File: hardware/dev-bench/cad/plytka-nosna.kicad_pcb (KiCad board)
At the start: 2 copper layers, 170 x 100 mm, 69 parts, among them J1 ARDUINO POWER, J10 CC1120EM P2, J11 ANALIZATOR, J12 VTEST 0-15V, J2 ARDUINO A0-A5, J3 ARDUINO D0-D7, J4 ARDUINO D8-SCL, J5 DEVKITC J1, J6 DEVKITC J3, J7 SHARP LS027B7DH01A, J9 CC1120EM P1, Q1 MMBT3904, SW1 GÓRA, SW2 DÓŁ, SW3 OK, SW4 WSTECZ, SW5 CISZA, SW6 PRZYGOTOWANIE, U1 CY15B104QN-50SXI, U2 MCP1640

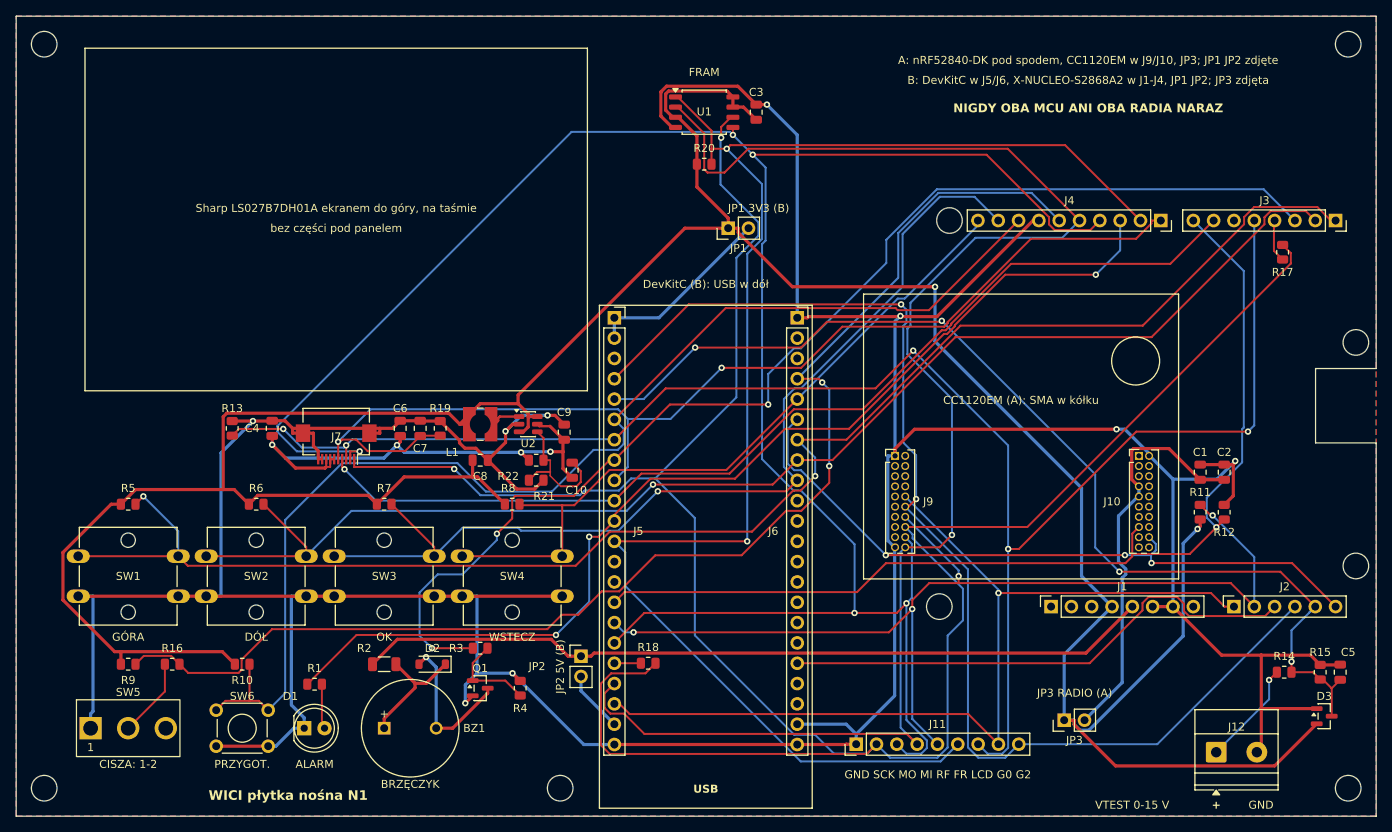
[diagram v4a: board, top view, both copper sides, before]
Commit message: Dev bench N1: hardware FRAM CS release on supply loss (audit vs F106)
The spec (elektronika.md, power loss, point 2) requires the FRAM CS to be
released before the FRAM supply drops below its minimum. The Arduino
RESET pin of the nRF52840-DK is not connected to the MCU (R45 not
fitted), so a supervisor on the MCU reset cannot do it on bench A.

- U3 TPS3840PH27 (push-pull active-high, 2.66-2.74 V) and U4 74LVC1G32
  force CS of U1 high below the threshold, independent of the MCU;
  C11/C12 decoupling; own TPS3840PH symbol (library WICI)
- bring-up steps F1-F3 (margin at 3.0 V, MR test, scope at power-off)
- docs: panel 5 V row in the supply table, 0.18 mm minimum track for
  the fabricator, SMD count, availability, reproduction record

Co-Authored-By: Claude Opus 5.5 <noreply@anthropic.com>
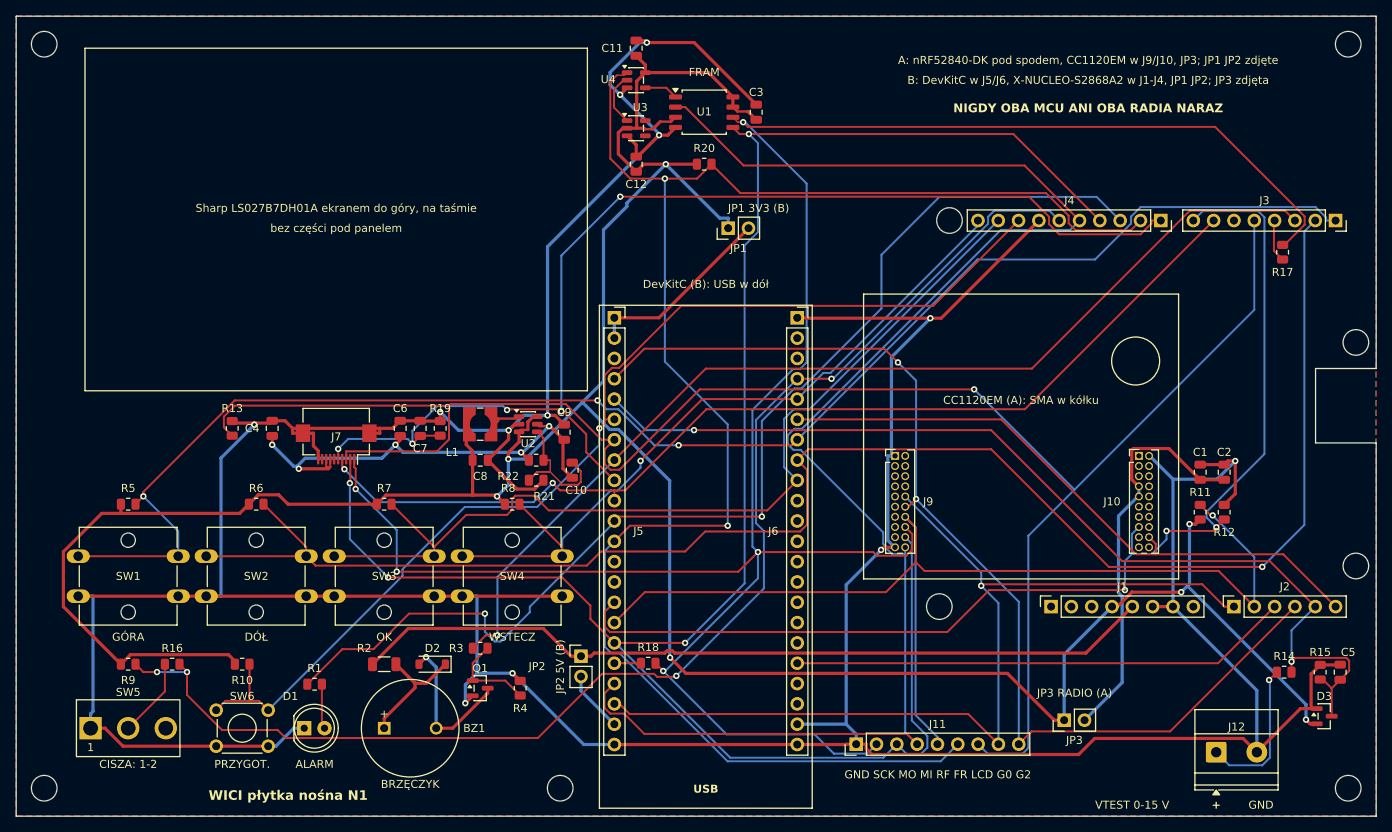
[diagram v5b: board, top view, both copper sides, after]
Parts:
- added C11: 100n, Capacitor_SMD:C_0805_2012Metric, F.Cu at (107.5, 34.0)
- added C12: 100n, Capacitor_SMD:C_0805_2012Metric, F.Cu at (107.5, 48.5)
- added U3: TPS3840PH27, Package_TO_SOT_SMD:SOT-23-5, F.Cu at (107.5, 44.0)
- added U4: 74LVC1G32, Package_TO_SOT_SMD:SOT-23-5, F.Cu at (107.5, 38.0)
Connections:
- U1 pad 1: /FRAM_CS -> /FRAM_CS_U1
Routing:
- net /GND: track 541.6 -> 596.1 mm, vias 9 -> 12
- net /BTN_DOWN: track 166.2 -> 205.8 mm
- net /SPI_MOSI: track 273.9 -> 250.9 mm, vias 5 -> 4
- net /SPI_SCK: track 302.2 -> 280.3 mm, vias 2 -> 5
- net /BUZZER: track 150.5 -> 130.2 mm, vias 3 -> 1
- net /RF_RESET: track 127.8 -> 145.5 mm, vias 1 -> 3
- net /FRAM_CS: track 194.1 -> 210.9 mm
- net /+3V3: track 389.6 -> 372.8 mm, vias 2 -> 7
- net /RF_GPIO2: track 149.5 -> 135.1 mm
- net /LCD_CS: track 215.1 -> 229.4 mm, vias 5 -> 1
- net /BTN_PREP: track 150.5 -> 137.6 mm, vias 0 -> 1
- net /LED_ALARM: track 133.1 -> 143.7 mm, vias 3 -> 2
- net /LCD_DISP: track 140.4 -> 149.4 mm, vias 2 -> 5
- net /RF_CS: track 129.8 -> 137.4 mm, vias 4 -> 1
- net /VTEST: track 132.1 -> 125.1 mm, vias 4 -> 2
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
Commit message: Dev bench N1: hold-up capacitor for the FRAM guard response time
TPS3840 asserts up to 30 us after +3V3 is 10 % below its threshold
(2.394 V worst case, SNVSB03E table 6.6). With only the 0805 parts on
N1, +3V3 at 150 mA would reach the 2.0 V FRAM minimum in about 16 us.
C13 100 uF 10 V X5R 1210 (>= 32 uF after DC bias and tolerance) keeps
the 2.394-2.0 V fall at >= 100 us, 3.4x the supervisor delay.

F3 now checks the fall rate (<= 6.6 mV/us), CS high within 30 us of
2.394 V with +3V3 still >= 2.2 V, under the largest +3V3 load.

Co-Authored-By: Claude Opus 5.5 <noreply@anthropic.com>
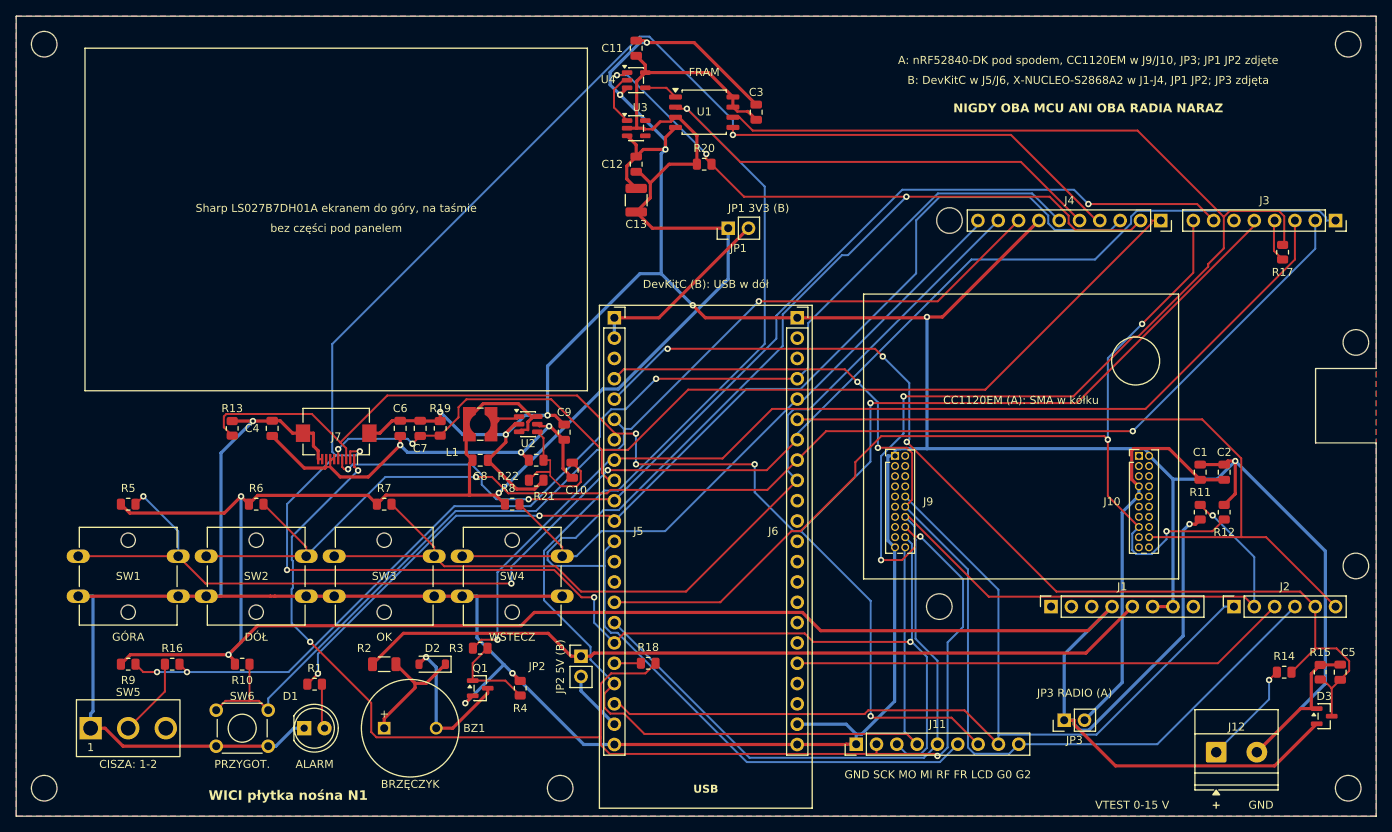
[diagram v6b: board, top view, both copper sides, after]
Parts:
- added C13: 100u, Capacitor_SMD:C_1210_3225Metric, F.Cu at (107.5, 53.0)
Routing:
- net /+3V3: track 372.8 -> 428.5 mm, vias 7 -> 4
- net /SPI_SCK: track 280.3 -> 321.9 mm, vias 5 -> 6
- net /BTN_DOWN: track 205.8 -> 168.5 mm, vias 1 -> 2
- net /SPI_MOSI: track 250.9 -> 276.5 mm, vias 4 -> 5
- net /SPI_MISO: track 196.1 -> 218.2 mm, vias 0 -> 1
- net /LCD_DISP: track 149.4 -> 127.5 mm, vias 5 -> 2
- net /LCD_CS: track 229.4 -> 212.5 mm, vias 1 -> 5
- net /SW_CISZA: track 164.7 -> 147.9 mm, vias 4 -> 3
- net /GND: track 596.1 -> 612.4 mm
- net /RF_GPIO3: track 79.5 -> 94.3 mm
- net /RF_RESET: track 145.5 -> 133.2 mm
- net /LED_ALARM: track 143.7 -> 135.5 mm
- net /VTEST: track 125.1 -> 132.3 mm, vias 2 -> 3
- net /VTEST_IN: track 18.9 -> 13.1 mm
- net /RF_CS: track 137.4 -> 142.1 mm
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
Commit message: N1.1: J7 odsunięte od panelu dla taśmy FPC 13,5 mm (F118)
FPC_GAP 9,7 mm (13,5 mm taśmy minus 3,8 mm w złączu FH12). J7 z R13,
R19, C4, C6, C7 o 7,4 mm dalej od panelu; rząd R5-R8 1,5 mm niżej (R7
na prawo od J7), SW1-SW4 i elementy pod nimi 2,0 mm niżej. R17 i R18
odsunięte od padów THT na >= 2,5 mm (montaż mieszany JLC; najmniej
2,73 mm). Nowa asercja: nic pod płaską taśmą FPC.

Płytka przetrasowana (Freerouting 2.5.0, 0 niepoprowadzonych), ERC 0,
DRC 0 z kanarkiem, odtworzenie w osobnej kopii bez różnic. Paczka
fabrication/N1 z rewizją N1.1, wycena JLC L0 i PDF-y dla wykonawcy
wygenerowane ponownie. Przymiarka 1:1 N1.1 zostaje otwarta.

Signed-off-by: Tomek Mierzwa <16899265+tmierzwa@users.noreply.github.com>
Co-Authored-By: Claude Opus 5.5 <noreply@anthropic.com>
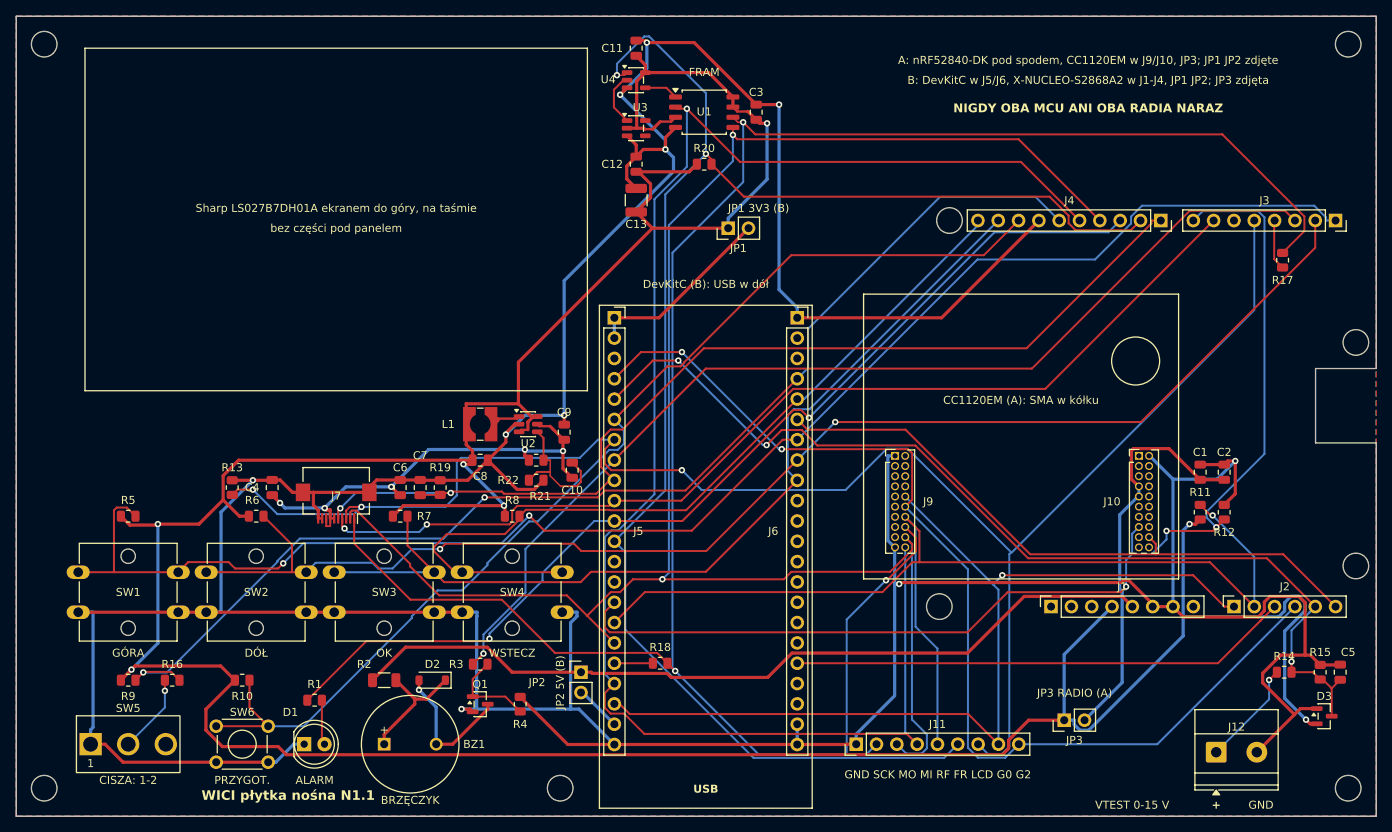
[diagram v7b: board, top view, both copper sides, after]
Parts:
- moved C4 7.40 mm to (62.0, 88.9)
- moved C6 7.40 mm to (78.0, 88.9)
- moved C7 7.40 mm to (80.5, 88.9)
- moved J7 7.40 mm to (70.0, 90.9)
- moved R13 7.40 mm to (57.0, 88.9)
- moved R19 7.40 mm to (83.0, 88.9)
- moved R7 2.50 mm to (78.0, 92.5)
- moved BZ1 2.00 mm to (76.0, 121.0)
- moved D1 2.00 mm to (66.0, 121.0)
- moved D2 2.00 mm to (82.0, 113.0)
- moved JP2 2.00 mm to (100.6, 112.0)
- moved Q1 2.00 mm to (88.0, 116.0)
- moved R1 2.00 mm to (67.3, 115.5)
- moved R10 2.00 mm to (58.2, 113.0)
- moved R16 2.00 mm to (49.5, 113.0)
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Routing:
- net /SPI_SCK: track 321.9 -> 267.1 mm, vias 6 -> 3
- net /SPI_MOSI: track 276.5 -> 229.4 mm, vias 5 -> 2
- net /+3V3: track 428.5 -> 446.9 mm, vias 4 -> 7
- net /SPI_MISO: track 218.2 -> 203.1 mm
- net /RF_GPIO3: track 94.3 -> 79.5 mm
- net /FRAM_CS: track 213.5 -> 199.3 mm, vias 3 -> 2
- net /BTN_BACK: track 90.9 -> 103.2 mm
- net /RF_RESET: track 133.2 -> 145.4 mm
- net /GND: track 612.4 -> 602.3 mm, vias 12 -> 10
- net /VTEST: track 132.3 -> 124.2 mm
- net /LCD_CS: track 212.5 -> 205.1 mm, vias 5 -> 3
- net /LED_ALARM: track 135.5 -> 128.2 mm
- net /LCD_EXTCOMIN: track 132.2 -> 127.1 mm, vias 3 -> 2
- net /RF_CS: track 142.1 -> 137.6 mm
- net /RF_GPIO0: track 122.3 -> 118.1 mm, vias 0 -> 1
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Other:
- board text added: "WICI płytka nośna N1.1"
- board text removed: "WICI płytka nośna N1"
